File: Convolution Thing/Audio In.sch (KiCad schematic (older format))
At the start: 75 parts

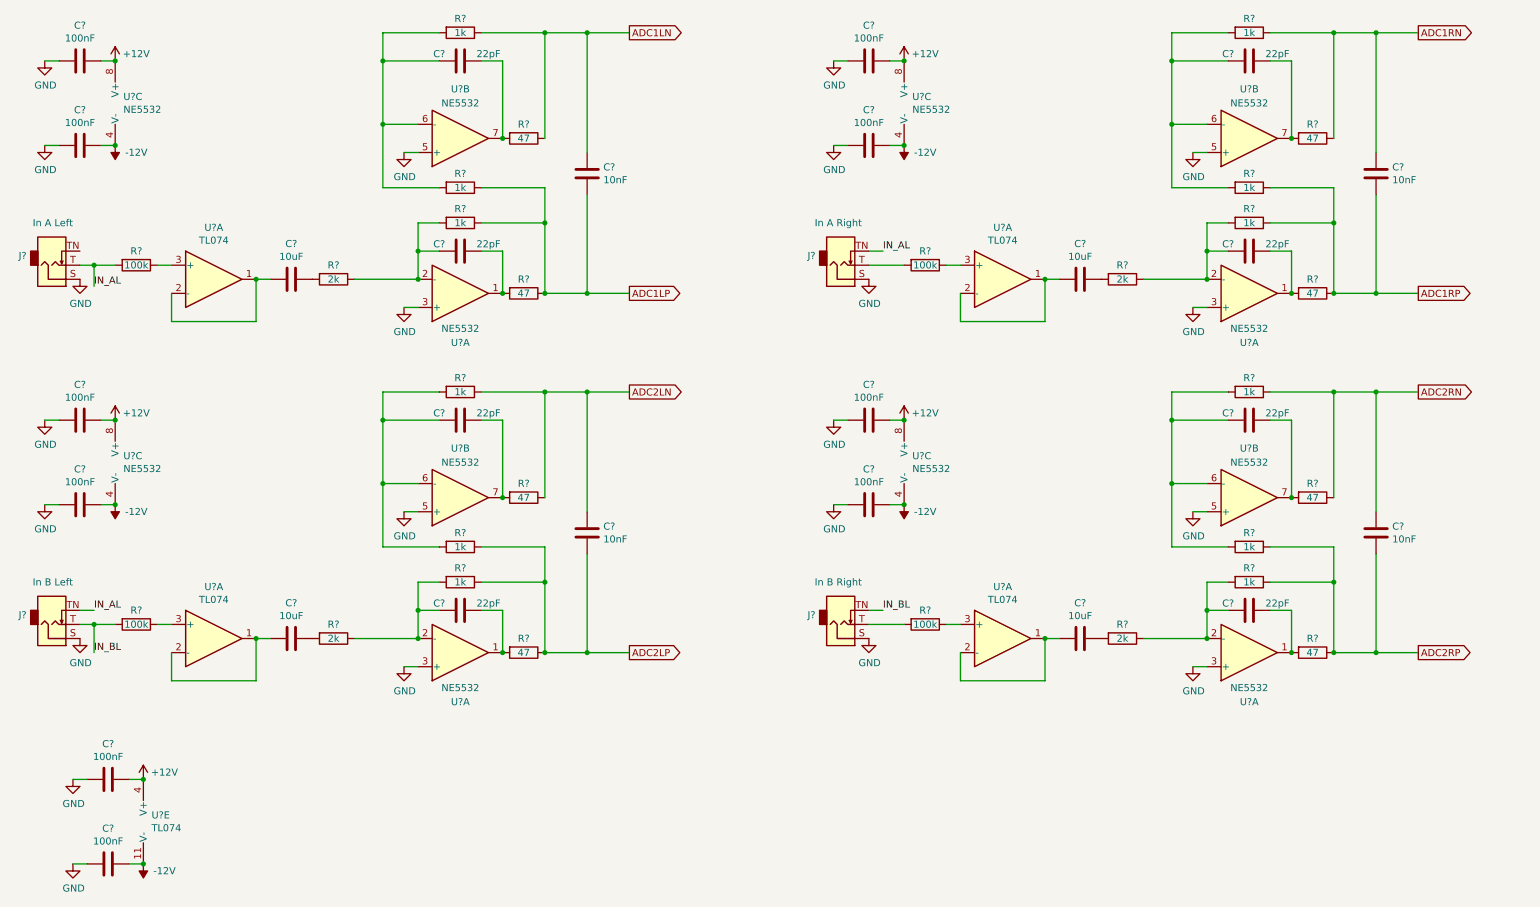
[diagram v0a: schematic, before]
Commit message: Work on CODEC and In/Out stages
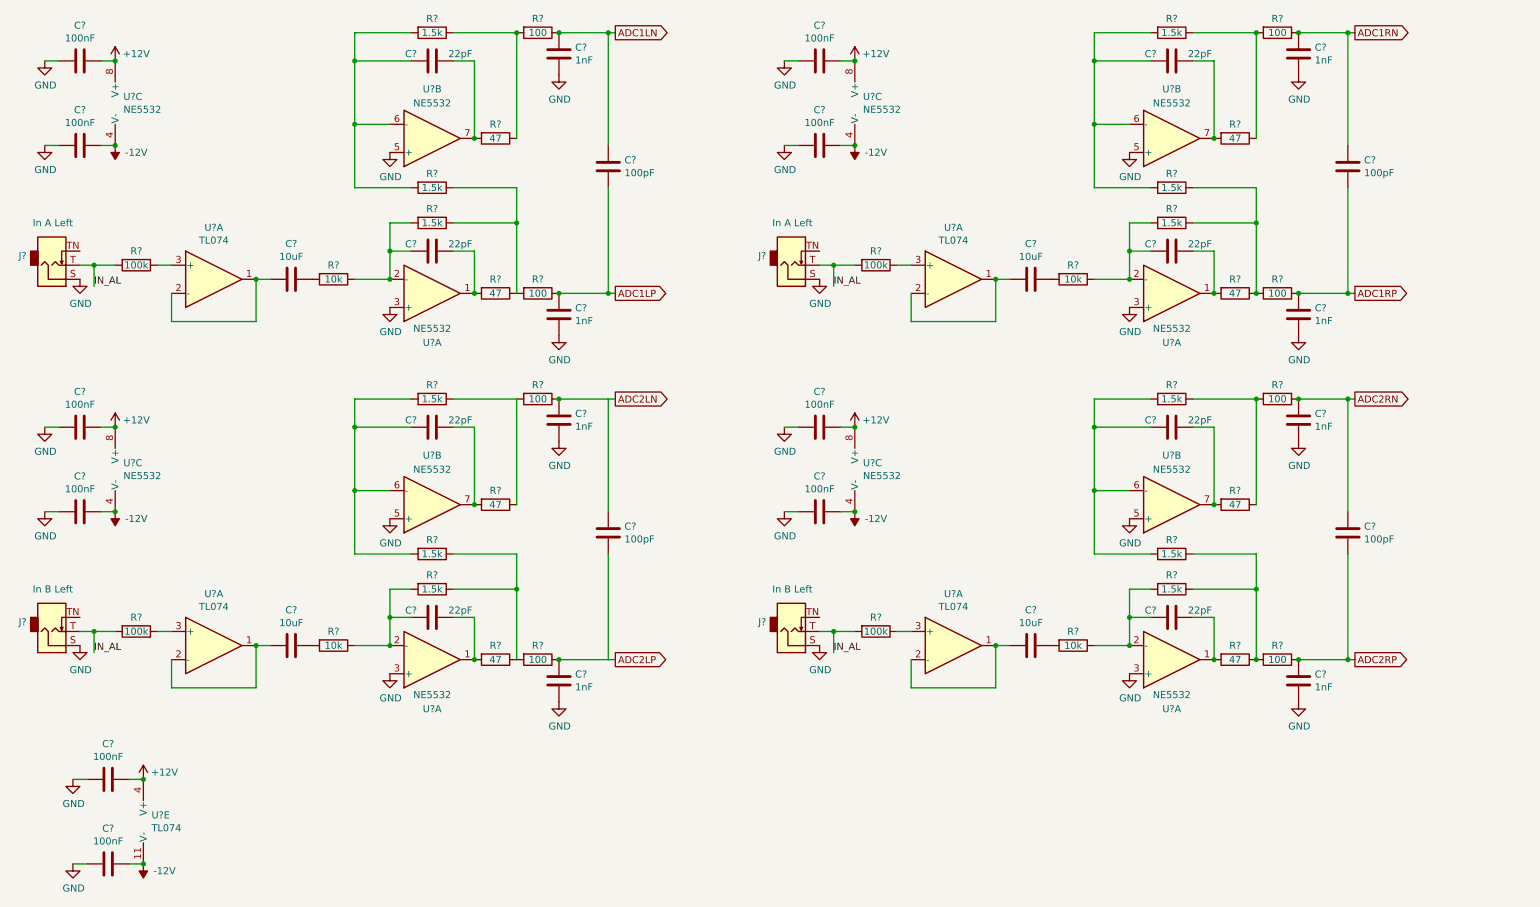
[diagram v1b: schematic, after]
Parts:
- removed C? (x3): 10uF, symbol Device:C
- removed C? (x6): 22pF, symbol Device:C
- removed C? (x3): 10nF, symbol Device:C
- removed C? (x6): 100nF, symbol Device:C
- removed J?: In B Left, symbol Connector:AudioJack2_SwitchT
- removed J?: In A Right, symbol Connector:AudioJack2_SwitchT
- removed J?: In B Right, symbol Connector:AudioJack2_SwitchT
- removed R? (x3): 100k, symbol Device:R
- removed R? (x3): 2k, symbol Device:R
- removed R? (x6): 47, symbol Device:R
- removed R? (x9): 1k, symbol Device:R
- removed U? (x3): TL074, symbol Amplifier_Operational:TL074
- removed U? (x9): NE5532, symbol Amplifier_Operational:NE5532
- added C? (x6): 100nF, symbol Device:C
- added C? (x3): 10uF, symbol Device:C
- added C? (x6): 22pF, symbol Device:C
- added C? (x3): 100pF, symbol Device:C
- added C? (x8): 1nF, symbol Device:C
- added J? (x2): In B Left, symbol Connector:AudioJack2_SwitchT
- added J?: In A Left, symbol Connector:AudioJack2_SwitchT
- added R? (x3): 100k, symbol Device:R
- added R? (x3): 10k, symbol Device:R
- added R? (x6): 47, symbol Device:R
- added R? (x9): 1.5k, symbol Device:R
- added R? (x8): 100, symbol Device:R
- added U? (x9): NE5532, symbol Amplifier_Operational:NE5532
- added U? (x3): TL074, symbol Amplifier_Operational:TL074
- C?: value 10nF -> 100pF
- R?: value 2k -> 10k
- R? (x3): value 1k -> 1.5k
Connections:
- net +12V: now also C?.1, C?.1, C?.1, U?.8 (V+), U?.8 (V+), U?.8 (V+)
- net -12V: now also C?.1, C?.1, C?.1, U?.4 (V-), U?.4 (V-), U?.4 (V-)
- net ADC1LN: now also C?.1, R?.1; no longer R?.1, R?.1
- net ADC1LP: now also C?.1, R?.1; no longer R?.1, R?.1, R?.1
- net ADC1RN: now also C?.1, C?.1, R?.1
- net ADC1RP: now also C?.1, C?.2, R?.1
- net ADC2LN: now also C?.1, C?.1, R?.1
- net ADC2LP: now also C?.1, C?.2, R?.1
- net ADC2RN: now also C?.1, C?.1, R?.1
- net ADC2RP: now also C?.1, C?.2, R?.1
- net GND: now also C?.2, C?.2, C?.2, C?.2, C?.2, C?.2, C?.2, C?.2, C?.2, C?.2, C?.2, C?.2, C?.2, C?.2, J?.S, J?.S, J?.S, U?.3 (+), U?.3 (+), U?.3 (+), U?.5 (+), U?.5 (+), U?.5 (+)
- net IN_AL: now also J?.T, J?.T, J?.T, R?.2, R?.2, R?.2
- new net: R?.1, U?.3 (+) (x3)
- new net: C?.2, U?.1, U?.2 (-) (x3)
- new net: C?.2, R?.1, R?.2, U?.2 (-) (x3)
- new net: C?.1, R?.2 (x3)
- new net: C?.1, R?.2, U?.1 (x3)
- new net: C?.2, R?.2, R?.2, U?.6 (-) (x3)
- new net: C?.1, R?.2, U?.7 (x3)
- new net: R?.1, R?.1, R?.1, R?.2 (x4)
- new net: R?.1, R?.1, R?.2 (x4)
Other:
- moved on the sheet: C?, R?, U?A, U?B

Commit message: New stereo codec and related changes. RIP multi-channel audio.
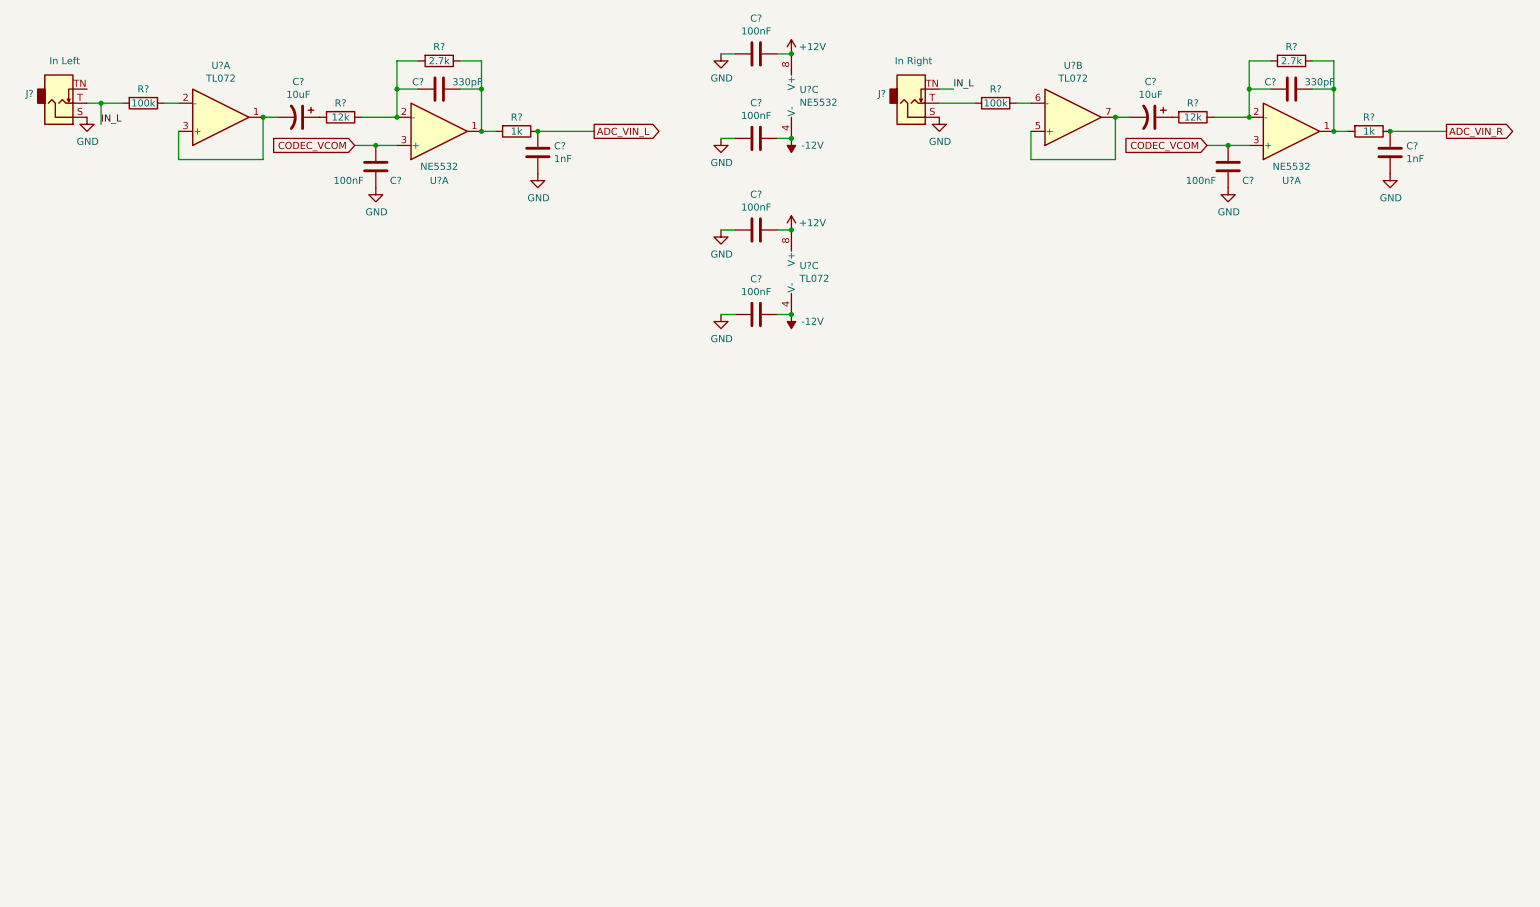
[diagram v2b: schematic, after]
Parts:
- removed C? (x4): 10uF, symbol Device:C
- removed C? (x8): 100nF, symbol Device:C
- removed C? (x7): 22pF, symbol Device:C
- removed C? (x4): 100pF, symbol Device:C
- removed C? (x7): 1nF, symbol Device:C
- removed J? (x2): In B Left, symbol Connector:AudioJack2_SwitchT
- removed J?: In A Left, symbol Connector:AudioJack2_SwitchT
- removed R? (x3): 100k, symbol Device:R
- removed R? (x3): 10k, symbol Device:R
- removed R? (x8): 47, symbol Device:R
- removed R? (x11): 1.5k, symbol Device:R
- removed R? (x7): 100, symbol Device:R
- removed U? (x5): TL074, symbol Amplifier_Operational:TL074
- removed U? (x10): NE5532, symbol Amplifier_Operational:NE5532
- added C? (x2): 10uF, symbol Device:CP1
- added C? (x4): 100nF, symbol Device:C
- added C?: 330pF, symbol Device:C
- added C?: 1nF, symbol Device:C
- added J?: In Right, symbol Connector:AudioJack2_SwitchT
- added R?: 100k, symbol Device:R
- added R?: 12k, symbol Device:R
- added R?: 2.7k, symbol Device:R
- added R?: 1k, symbol Device:R
- added U?: NE5532, symbol Amplifier_Operational:NE5532
- added U? (x3): TL072, symbol Amplifier_Operational:TL072
- C?: value 22pF -> 330pF
- J?: value In A Left -> In Left
- R?: value 10k -> 12k
- R?: value 1.5k -> 2.7k
- R?: value 100 -> 1k
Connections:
- net +12V: now also C?.1, U?.8 (V+)
- net -12V: now also C?.1, U?.4 (V-)
- net GND: now also C?.1, C?.1, C?.2, C?.2, C?.2, J?.S; no longer U?.3 (+)
- net at R?.1: now also U?.2 (-)
- net at R?.2: now also C?.1
- net at C?.1, U?.1: now also R?.1, R?.2
- net ADC1LP renamed ADC_VIN_L
- net IN_AL renamed IN_L
- net IN_L: now also J?.TN
- new net: C?.2, U?.1, U?.3 (+)
- new net: J?.T, R?.2
- new net: R?.1, U?.6 (-)
- new net: C?.2, R?.1, R?.2, U?.2 (-)
- new net: C?.1, R?.2
- new net: C?.1, R?.1, R?.2, U?.1
- new net: C?.2, U?.5 (+), U?.7
- new net ADC_VIN_R: C?.1, R?.1
- new net CODEC_VCOM: C?.2, C?.2, U?.3 (+), U?.3 (+)
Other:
- moved on the sheet: C?, J?, R?, U?A, U?C

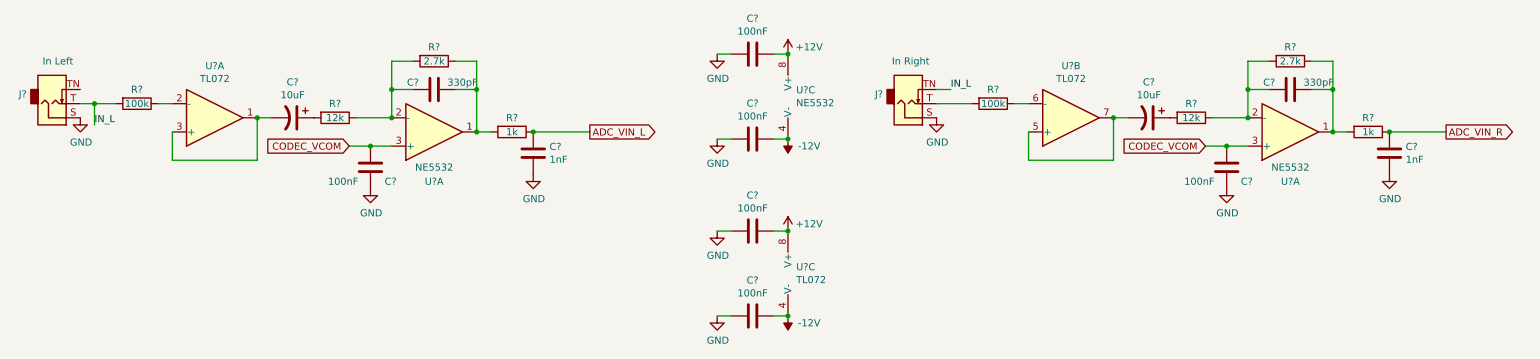
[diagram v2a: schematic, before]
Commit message: Audio I/O, CV input, GPIO work & misc changes
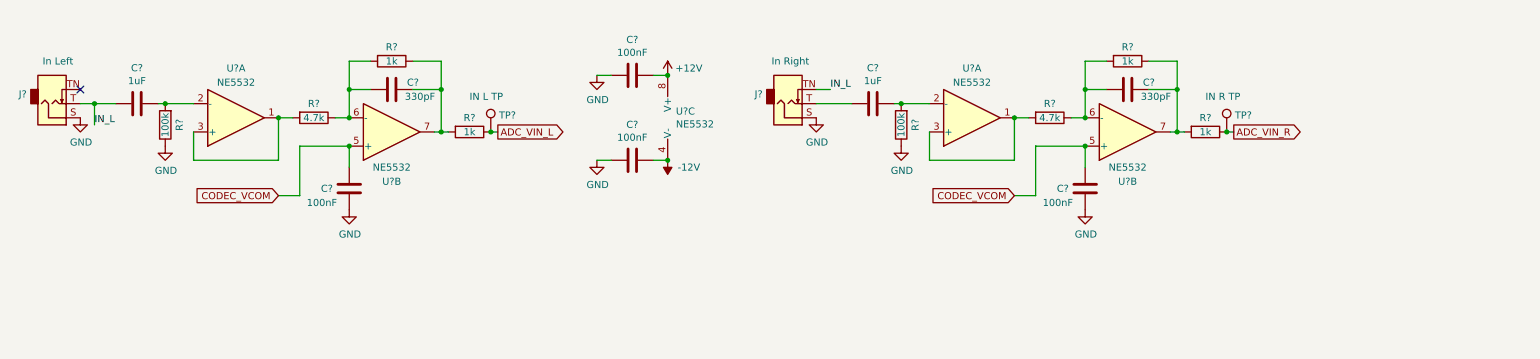
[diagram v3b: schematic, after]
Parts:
- removed C? (x2): 10uF, symbol Device:CP1
- removed C?: 330pF, symbol Device:C
- removed C? (x2): 1nF, symbol Device:C
- removed C? (x3): 100nF, symbol Device:C
- removed J?: In Right, symbol Connector:AudioJack2_SwitchT
- removed R?: 100k, symbol Device:R
- removed R?: 12k, symbol Device:R
- removed R?: 2.7k, symbol Device:R
- removed R?: 1k, symbol Device:R
- removed U?: NE5532, symbol Amplifier_Operational:NE5532
- removed U? (x3): TL072, symbol Amplifier_Operational:TL072
- added C? (x2): 1uF, symbol Device:C
- added C?: 100nF, symbol Device:C
- added C?: 330pF, symbol Device:C
- added J?: In Right, symbol Connector:AudioJack2_SwitchT
- added R?: 100k, symbol Device:R
- added R?: 4.7k, symbol Device:R
- added R? (x2): 1k, symbol Device:R
- added TP?: IN L TP, symbol Connector:TestPoint
- added TP?: IN R TP, symbol Connector:TestPoint
- added U? (x3): NE5532, symbol Amplifier_Operational:NE5532
- R?: value 12k -> 4.7k
- R?: value 2.7k -> 1k
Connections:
- net ADC_VIN_L: now also TP?.1
- net ADC_VIN_R: now also R?.1, TP?.1
- net CODEC_VCOM: now also U?.5 (+), C?.2, U?.5 (+); no longer U?.3 (+)
- net GND: now also R?.1, C?.1, J?.S, R?.1
- net IN_L: now also C?.2, J?.TN; no longer R?.2
- net at C?.2, R?.1, R?.2: now also U?.6 (-); no longer U?.2 (-)
- net at R?.2: now also U?.1, U?.3 (+)
- net at C?.1, R?.1, R?.2: now also U?.7; no longer U?.1
- new net: C?.1, R?.2, U?.2 (-) (x2)
- new net: C?.2, J?.T
- new net: C?.2, R?.1, R?.2, U?.6 (-)
- new net: R?.2, U?.1, U?.3 (+)
- new net: C?.1, R?.1, R?.2, U?.7
- no-connect marks 0 -> 1
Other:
- moved on the sheet: C?, R?, U?C

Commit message: Fix some issues, add component references
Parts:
- added C34, C35: 100nF, symbol Device:C
- added unit 3 of U6
- gave numbers to parts that had none: 22
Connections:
- net +12V: now also C34.1, U6.8 (V+)
- net -12V: now also C35.1, U6.4 (V-)
- net GND: now also C34.2, C35.2

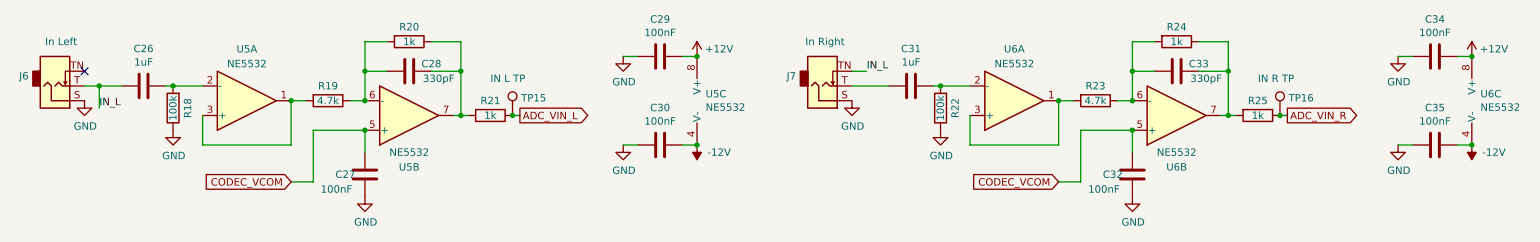
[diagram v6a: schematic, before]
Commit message: Assign all footprints
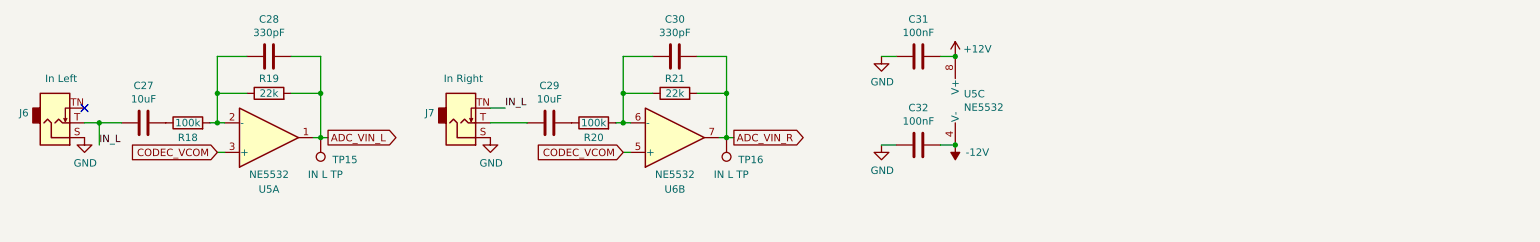
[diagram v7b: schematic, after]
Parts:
- removed C27, C32, C34, C35: 100nF, symbol Device:C
- removed C31: 1uF, symbol Device:C
- removed C33: 330pF, symbol Device:C
- removed R22: 100k, symbol Device:R
- removed R23: 4.7k, symbol Device:R
- removed R24, R25: 1k, symbol Device:R
- removed unit 2 of U5
- removed unit 3 of U6
- removed unit 1 of U6
- added C29: 10uF, Capacitor_SMD:C_0805_2012Metric, symbol Device:C
- added C30: 330pF, Capacitor_SMD:C_0805_2012Metric, symbol Device:C
- C27: renamed from C26; value 1uF -> 10uF; footprint (none) -> Capacitor_SMD:C_0805_2012Metric
- C28: footprint (none) -> Capacitor_SMD:C_0805_2012Metric
- C31: renamed from C29; footprint (none) -> Capacitor_SMD:C_0805_2012Metric
- C32: renamed from C30; footprint (none) -> Capacitor_SMD:C_0805_2012Metric
- J6, J7: footprint (none) -> SamacSys:ACJMNV352S
- R18: footprint (none) -> Resistor_SMD:R_0805_2012Metric
- R19: value 4.7k -> 22k; footprint (none) -> Resistor_SMD:R_0805_2012Metric
- R20: value 1k -> 100k; footprint (none) -> Resistor_SMD:R_0805_2012Metric
- R21: value 1k -> 22k; footprint (none) -> Resistor_SMD:R_0805_2012Metric
- TP15: footprint (none) -> TestPoint:TestPoint_Loop_D2.60mm_Drill1.6mm_Beaded
- TP16: value IN R TP -> IN L TP; footprint (none) -> TestPoint:TestPoint_Loop_D2.60mm_Drill1.6mm_Beaded
- U5, U6: footprint (none) -> Package_SO:SOIC-8_3.9x4.9mm_P1.27mm
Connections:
- net ADC_VIN_L: now also C28.1, R19.2, U5.1; no longer R21.1
- net ADC_VIN_R: now also R21.2, U6.7, C30.1
- net CODEC_VCOM: now also U5.3 (+)
- net GND: no longer R18.1
- net at R18.2, U5.2 (-): now also C28.2, R19.1; no longer C27.1
- net at J7.T: now also C29.2
- net at U6.6 (-): now also R20.2, R21.1, C30.2
- new net: C27.1, R18.1
- new net: C29.1, R20.1
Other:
- moved on the sheet: C27, C31, C32, J6, R18, TP15, U5A, U5C
